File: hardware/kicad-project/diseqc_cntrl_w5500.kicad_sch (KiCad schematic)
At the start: 30 parts, among them IC6 W5500, J8 RJCSE538101, T1 H1102NL, Y2 25MHZ

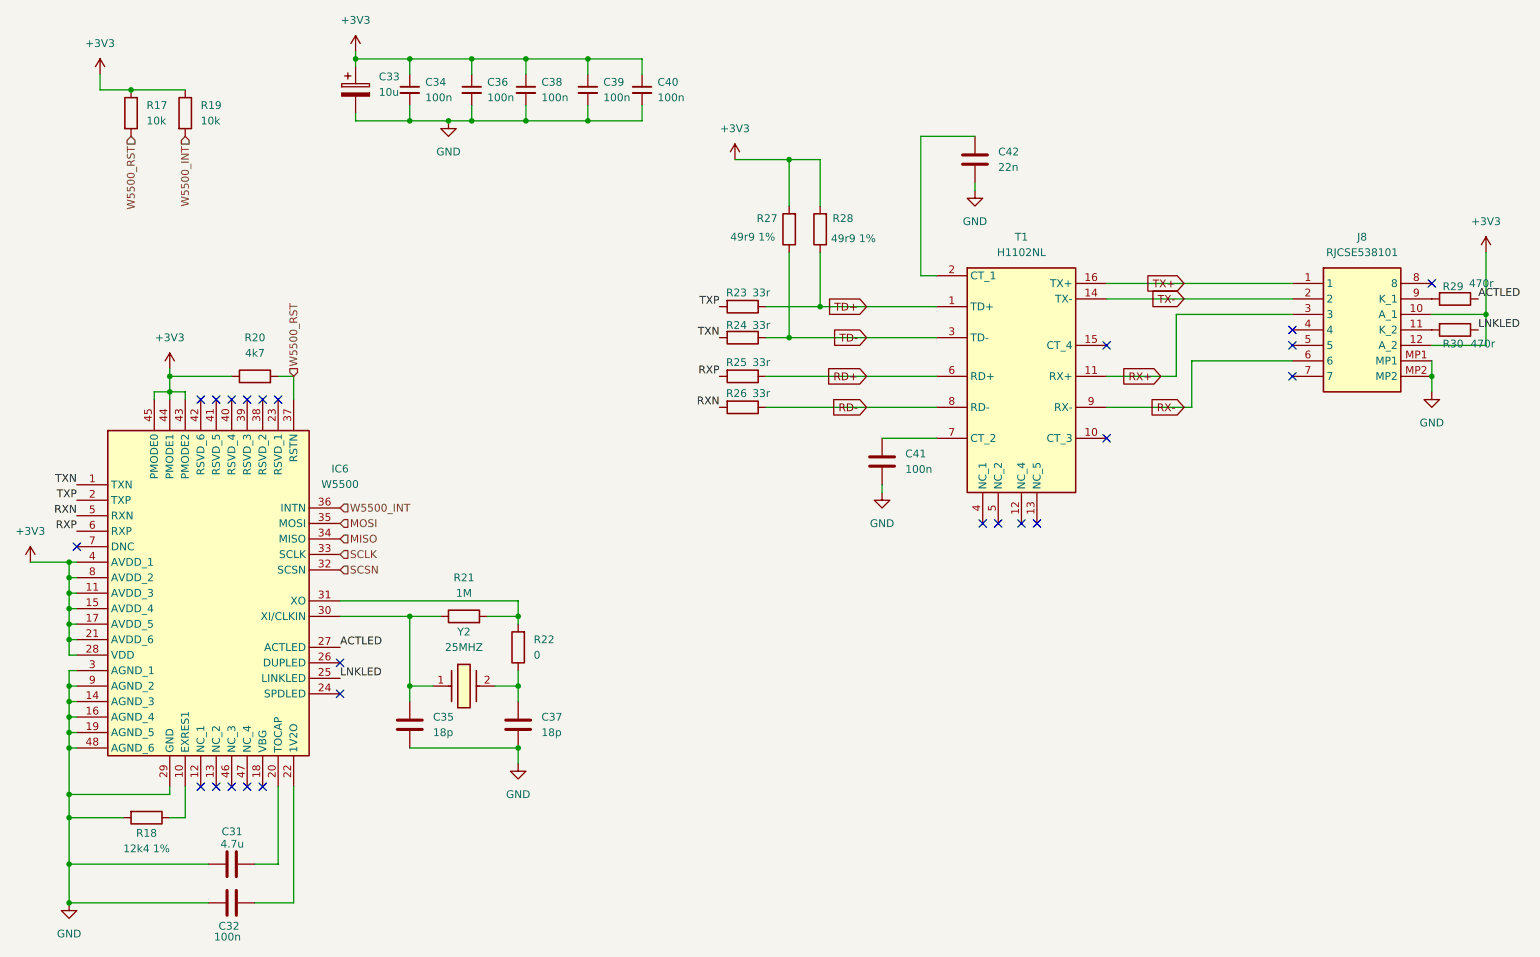
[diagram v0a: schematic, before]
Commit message: nwe board laylout for LAN8742A
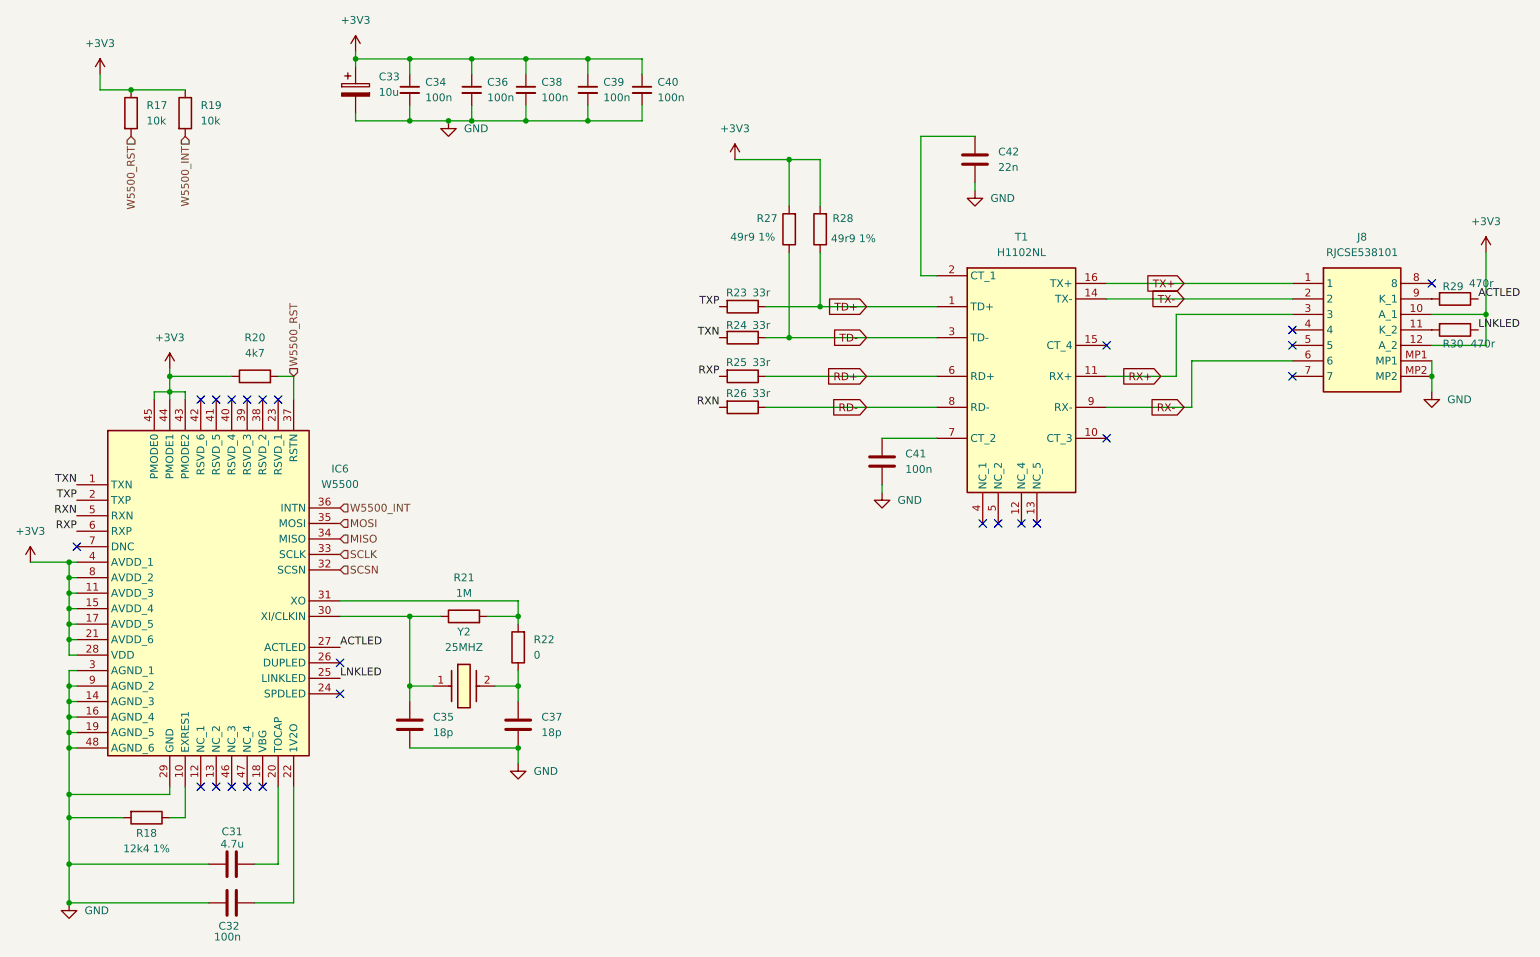
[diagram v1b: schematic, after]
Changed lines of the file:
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@@
 	)
 	(symbol
-		(lib_id "diseqc_cntrl:GND")
+		(lib_id "power:GND")
 		(at 88.9 33.02 0)
 		(unit 1)
@@
 		)
 		(property "Value" "GND"
-			(at 88.9 38.1 0)
+			(at 91.44 34.2899 0)
 			(show_name no)
 			(do_not_autoplace no)
@@
 					(size 1.27 1.27)
 				)
+				(justify left)
 			)
 		)
@@
 	)
 	(symbol
-		(lib_id "diseqc_cntrl:GND")
+		(lib_id "power:GND")
 		(at 100.33 138.43 0)
 		(unit 1)
@@
 		)
 		(property "Value" "GND"
-			(at 100.33 143.51 0)
+			(at 102.87 139.6999 0)
 			(show_name no)
 			(do_not_autoplace no)
@@
 					(size 1.27 1.27)
 				)
+				(justify left)
 			)
 		)
@@
 	)
 	(symbol
-		(lib_id "diseqc_cntrl:GND")
+		(lib_id "power:GND")
 		(at 160.02 93.98 0)
 		(unit 1)
@@
 		)
 		(property "Value" "GND"
-			(at 160.02 99.06 0)
+			(at 162.56 95.2499 0)
 			(show_name no)
 			(do_not_autoplace no)
@@
 					(size 1.27 1.27)
 				)
+				(justify left)
 			)
 		)
@@
 	)
 	(symbol
-		(lib_id "diseqc_cntrl:GND")
+		(lib_id "power:GND")
 		(at 175.26 44.45 0)
 		(unit 1)
@@
 		)
 		(property "Value" "GND"
-			(at 175.26 49.53 0)
+			(at 177.8 45.7199 0)
 			(show_name no)
 			(do_not_autoplace no)
@@
 					(size 1.27 1.27)
 				)
+				(justify left)
 			)
 		)
@@
 	)
 	(symbol
-		(lib_id "diseqc_cntrl:GND")
+		(lib_id "power:GND")
 		(at 26.67 161.29 0)
 		(unit 1)
@@
 		)
 		(property "Value" "GND"
-			(at 26.67 166.37 0)
+			(at 29.21 162.5599 0)
 			(show_name no)
 			(do_not_autoplace no)
@@
 					(size 1.27 1.27)
 				)
+				(justify left)
 			)
 		)
@@
 	)
 	(symbol
-		(lib_id "diseqc_cntrl:GND")
+		(lib_id "power:GND")
 		(at 250.19 77.47 0)
 		(unit 1)
@@
 		)
 		(property "Value" "GND"
-			(at 250.19 82.55 0)
+			(at 252.73 78.7399 0)
 			(show_name no)
 			(do_not_autoplace no)
@@
 					(size 1.27 1.27)
 				)
+				(justify left)
 			)
 		)
